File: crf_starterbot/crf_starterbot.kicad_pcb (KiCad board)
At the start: 2 copper layers, 48 parts, among them J101 Screw_Terminal_01x02, J102 Conn_01x10_Female, J103 Screw_Terminal_01x02, J104 Screw_Terminal_01x02, Q101 Q_NPN_BCE, SW101 SW_SPST, SW102 SW_SPST, SW103 SW_SPST, U101 WeMos_D1_mini, U103 LM393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

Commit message: Started layout considerations of the pcb
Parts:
- added U102: HC-SR04, Connector_PinHeader_2.54mm:PinHeader_1x04_P2.54mm_Vertical, F.Cu at (238.3, 192.5)
- moved U107 206.3 mm to (260.6, 253.5), turned to 270 degrees
- moved Q101 204.3 mm to (260.1, 195.6)
- moved J103 200.3 mm to (254.4, 245.8)
- moved U108 193.7 mm to (239.8, 255.0), turned to 270 degrees
- moved J104 191.3 mm to (234.1, 245.1)
- moved U101 185.5 mm to (205.7, 154.9), turned to 270 degrees
- moved SW101 184.2 mm to (175.3, 240.0)
- moved U103 171.5 mm to (154.4, 226.6)
- moved SW102 165.3 mm to (128.3, 242.6)
- moved SW103 163.6 mm to (231.6, 144.8)
- moved U104 154.6 mm to (170.2, 212.1)
- moved J102 144.8 mm to (207.0, 125.7), turned to 270 degrees
- moved C108 115.4 mm to (89.2, 207.3), turned to 180 degrees
- moved U106 114.5 mm to (138.4, 210.8)
- moved C101 106.8 mm to (89.7, 201.7), turned to 180 degrees
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
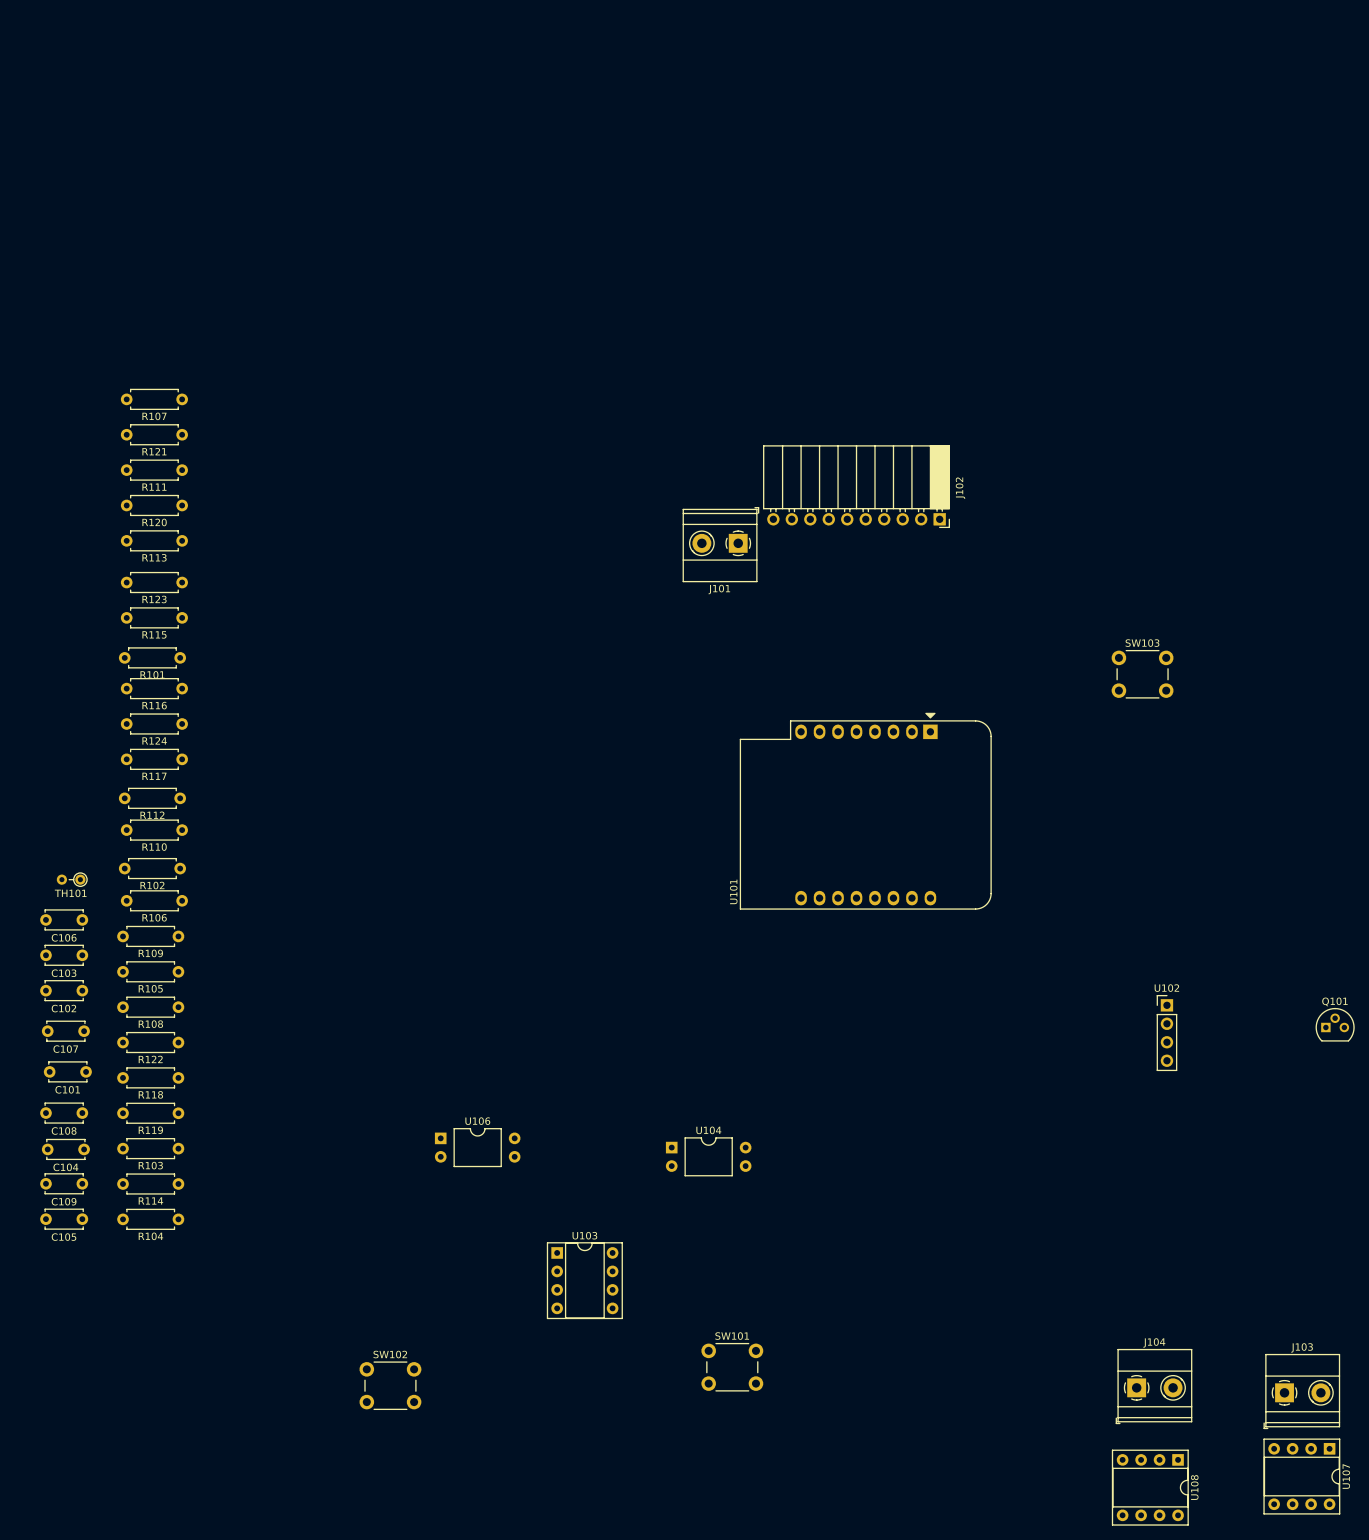
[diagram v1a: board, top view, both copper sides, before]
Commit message: Completed placement of components into functional units, begun routing
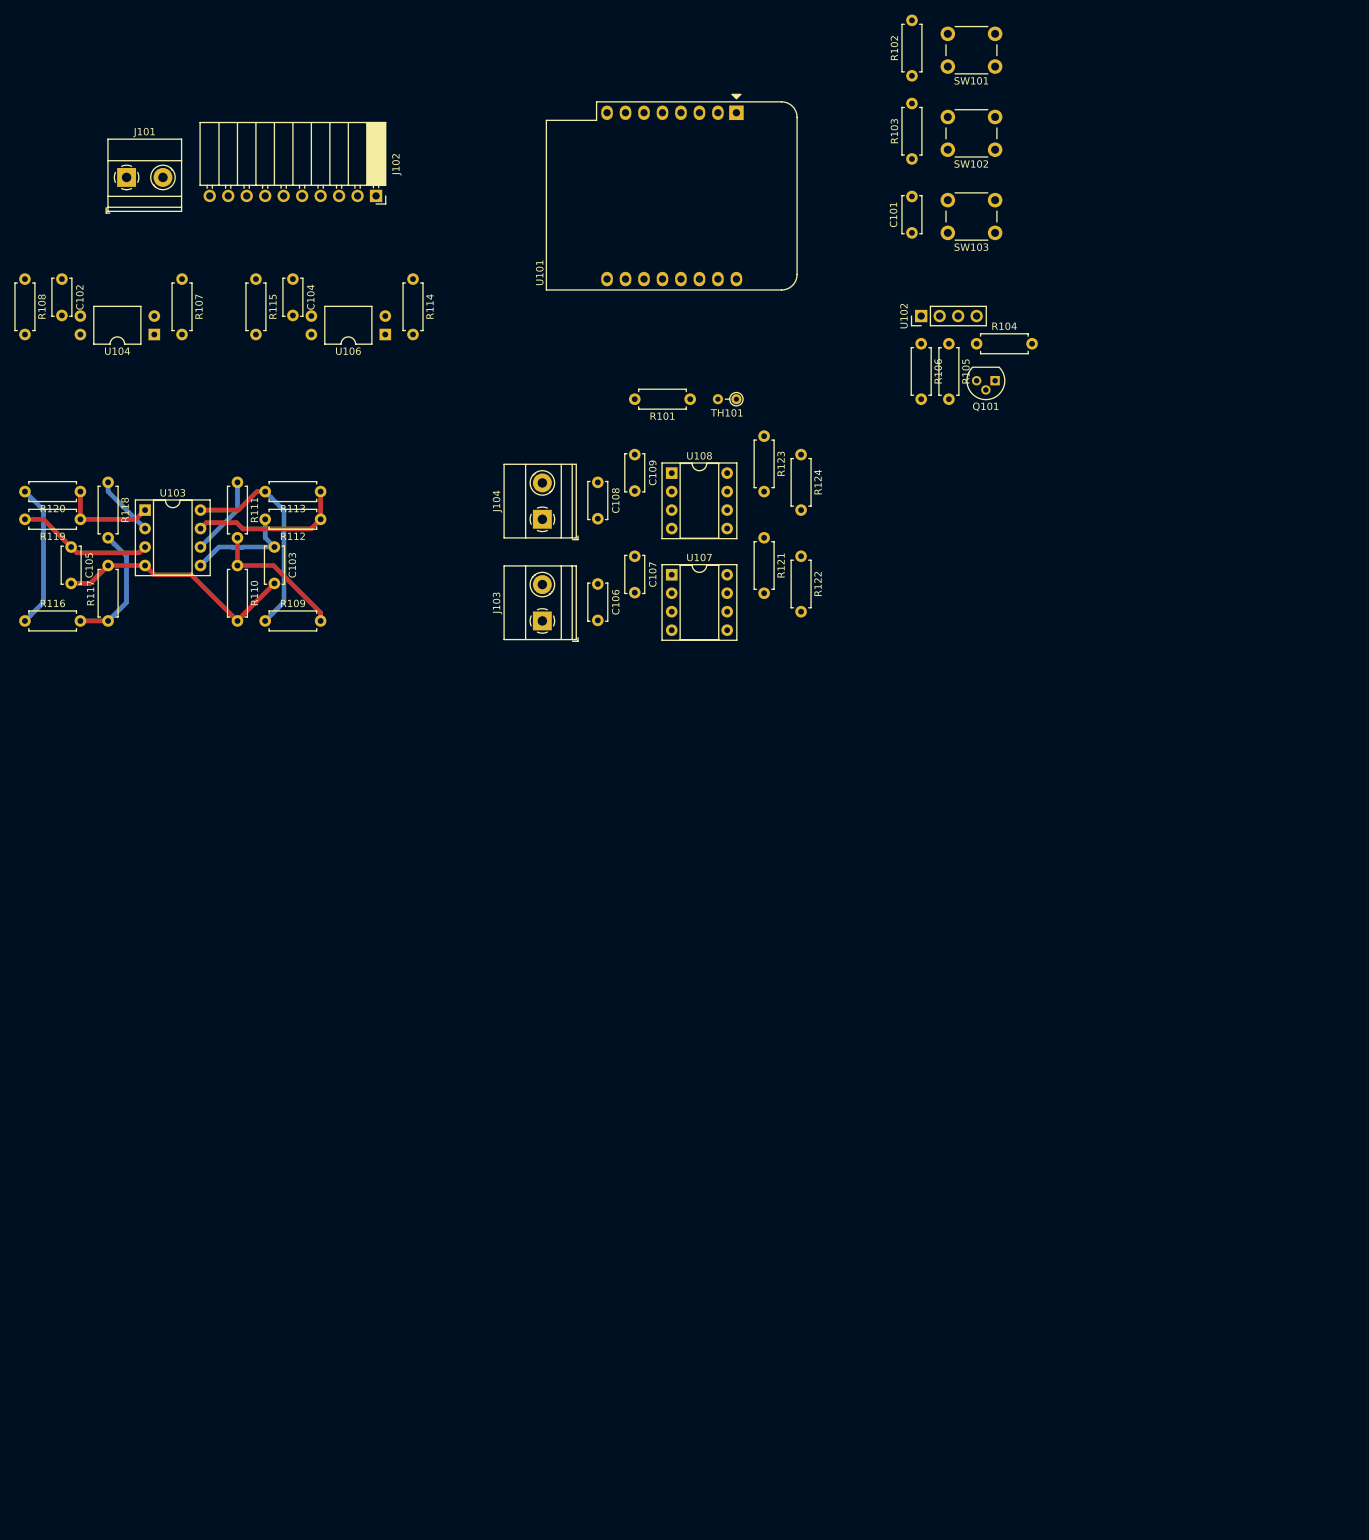
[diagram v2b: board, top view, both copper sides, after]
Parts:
- moved SW102 188.6 mm to (214.6, 74.9), turned to 180 degrees
- moved SW101 180.9 mm to (214.6, 63.5), turned to 180 degrees
- moved R103 169.3 mm to (203.2, 76.2), turned to 90 degrees
- moved R104 162.9 mm to (212.1, 101.6), turned to 0 degrees
- moved C101 161.8 mm to (203.2, 86.4), turned to 90 degrees
- moved U108 152.4 mm to (170.2, 119.4), turned to 0 degrees
- moved U107 150.4 mm to (170.2, 133.3), turned to 0 degrees
- moved R102 148.3 mm to (203.2, 64.8), turned to 90 degrees
- moved J103 147.2 mm to (152.4, 139.7), turned to 90 degrees
- moved J104 144.7 mm to (152.4, 125.7), turned to 90 degrees
- moved R105 136.6 mm to (208.3, 101.6), turned to 270 degrees
- moved U104 132.5 mm to (99.1, 100.3), turned to 180 degrees
- moved R114 128.5 mm to (134.6, 92.7), turned to 270 degrees
- moved R106 127.2 mm to (204.5, 101.6), turned to 270 degrees
- moved C109 125.7 mm to (165.1, 116.8), turned to 270 degrees
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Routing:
- net +3V3: track 0.00 -> 49.7 mm
- net GND: track 0.00 -> 34.3 mm
- net LEFT_ENC: track 0.00 -> 21.5 mm
- net Net-(R109-Pad2): track 0.00 -> 19.1 mm
- net Net-(C105-Pad1): track 0.00 -> 18.8 mm
- net Net-(R116-Pad2): track 0.00 -> 17.3 mm
- net Net-(C103-Pad1): track 0.00 -> 15.6 mm
- net RIGHT_ENC: track 0.00 -> 13.2 mm
- net Net-(R111-Pad1): track 0.00 -> 11.0 mm
- net Net-(R118-Pad1): track 0.00 -> 8.45 mm

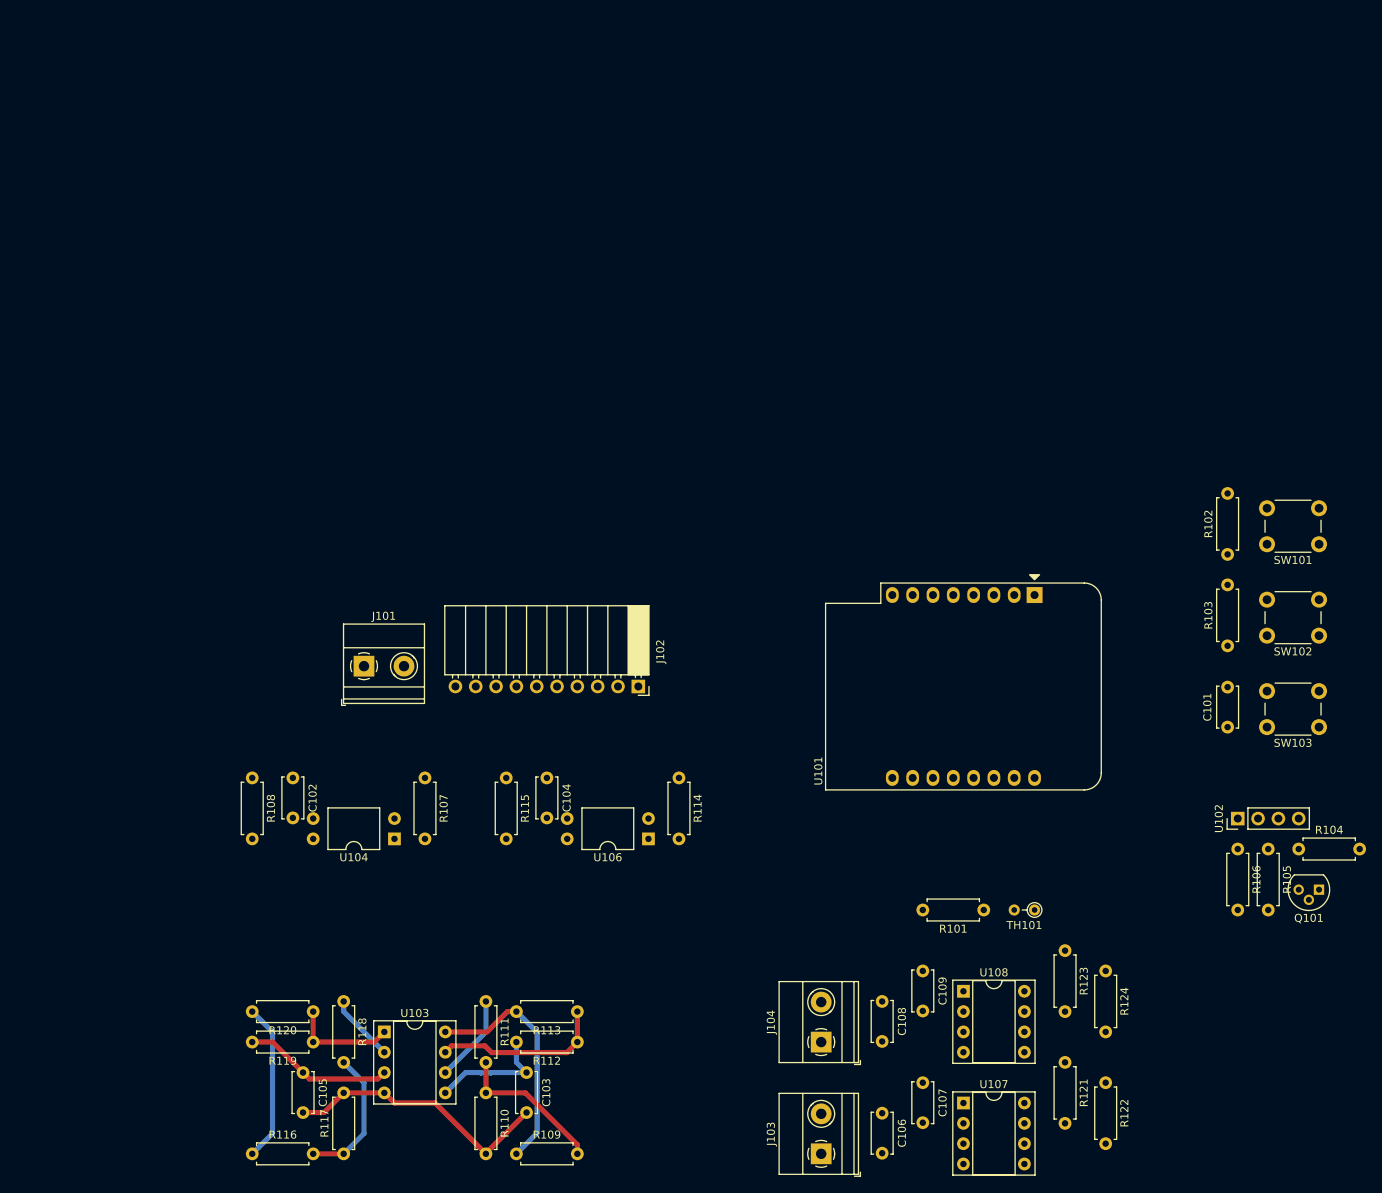
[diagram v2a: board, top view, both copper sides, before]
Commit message: State of board before proper placement of phototransistors and interconnection functional units
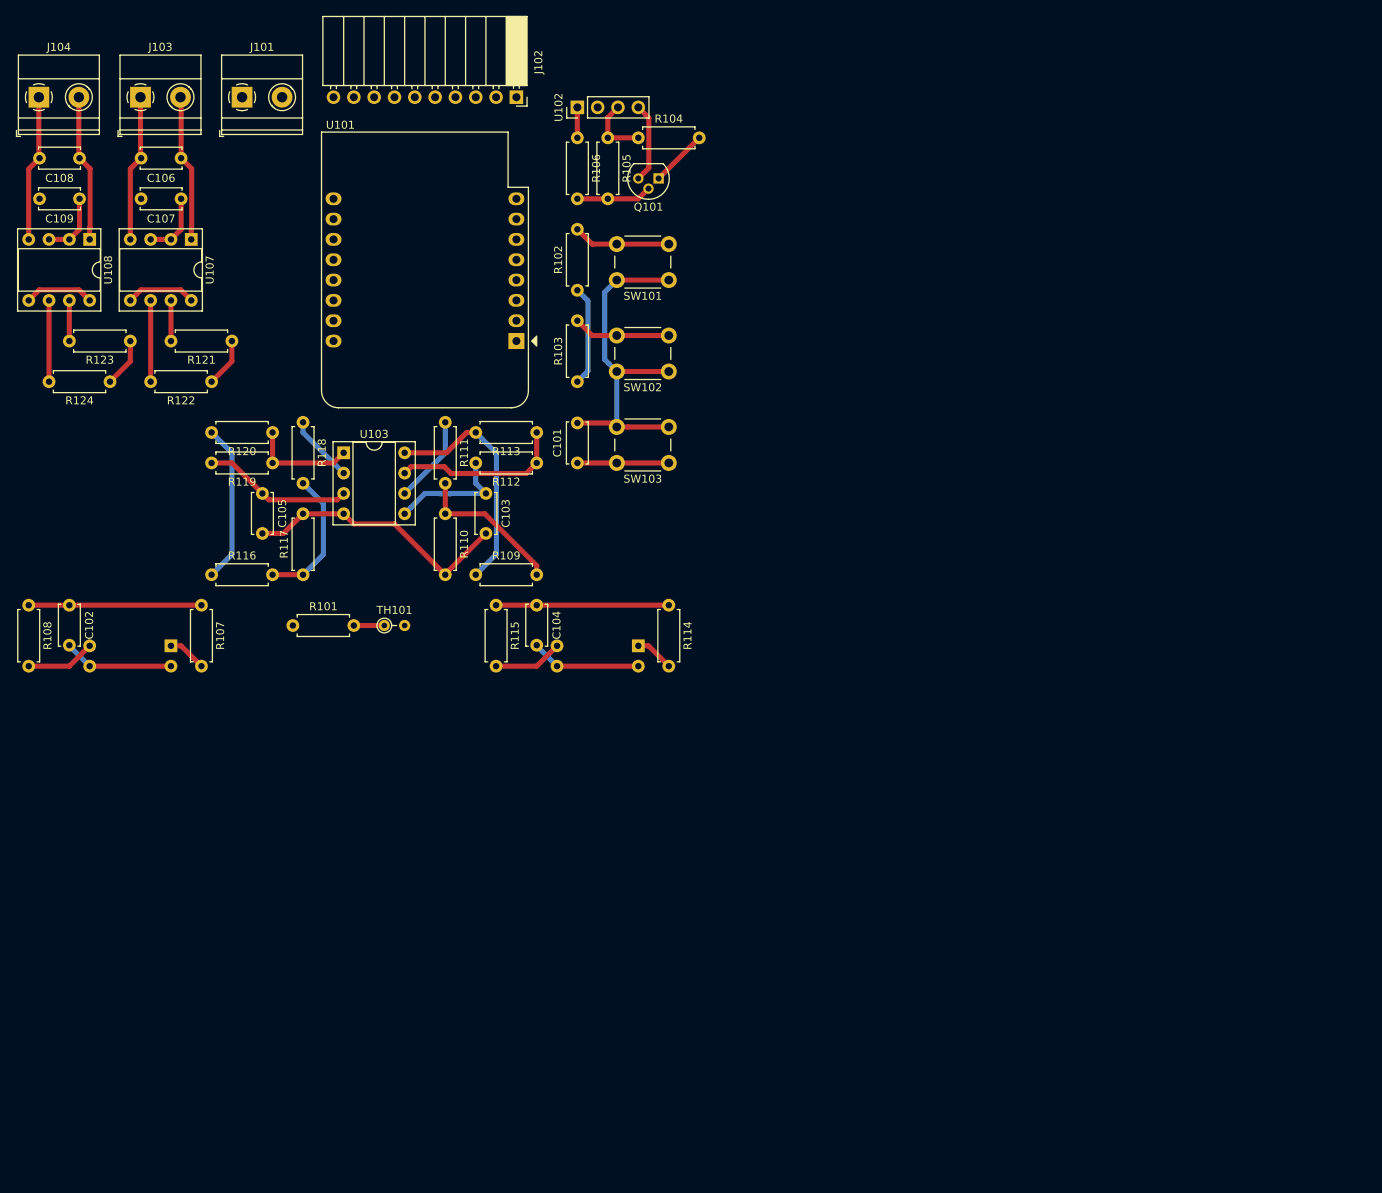
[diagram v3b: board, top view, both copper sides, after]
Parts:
- U104, U106: moved to B.Cu
- moved J103 157.1 mm to (67.3, 7.62), turned to 0 degrees
- moved J104 153.3 mm to (54.6, 7.62), turned to 0 degrees
- moved C106 148.1 mm to (72.4, 15.2), turned to 180 degrees
- moved C108 145.5 mm to (59.7, 15.2), turned to 180 degrees
- moved U107 144.8 mm to (73.7, 25.4), turned to 270 degrees
- moved R124 144.6 mm to (63.5, 43.2), turned to 180 degrees
- moved C107 144.2 mm to (72.4, 20.3), turned to 180 degrees
- moved U108 144.1 mm to (61.0, 25.4), turned to 270 degrees
- moved C109 142.9 mm to (59.7, 20.3), turned to 180 degrees
- moved R122 142.0 mm to (76.2, 43.2), turned to 180 degrees
- moved R123 139.5 mm to (66.0, 38.1), turned to 180 degrees
- moved R121 137.8 mm to (78.7, 38.1), turned to 180 degrees
- moved R104 121.3 mm to (129.5, 12.7)
- moved U102 121.3 mm to (121.9, 8.89)
- moved Q101 121.3 mm to (132.1, 17.8)
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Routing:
- net GND: track 34.3 -> 133.7 mm
- net +3V3: track 49.7 -> 121.5 mm
- net +BATT: track 0.00 -> 27.7 mm
- net Net-(C108-Pad1): track 0.00 -> 18.4 mm
- net Net-(C106-Pad1): track 0.00 -> 18.4 mm
- net Net-(C108-Pad2): track 0.00 -> 18.4 mm
- net Net-(C106-Pad2): track 0.00 -> 18.4 mm
- net LEFT_SW: track 0.00 -> 12.2 mm
- net RIGHT_SW: track 0.00 -> 12.2 mm
- net RIGHTA: track 0.00 -> 10.2 mm
- net LEFTA: track 0.00 -> 10.2 mm
- net ECHO: track 0.00 -> 9.42 mm
- net Net-(C103-Pad1): track 15.6 -> 24.3 mm
- net Net-(C105-Pad1): track 18.8 -> 27.4 mm
- net Net-(R104-Pad1): track 0.00 -> 8.15 mm
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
